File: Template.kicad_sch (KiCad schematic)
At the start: 0 parts

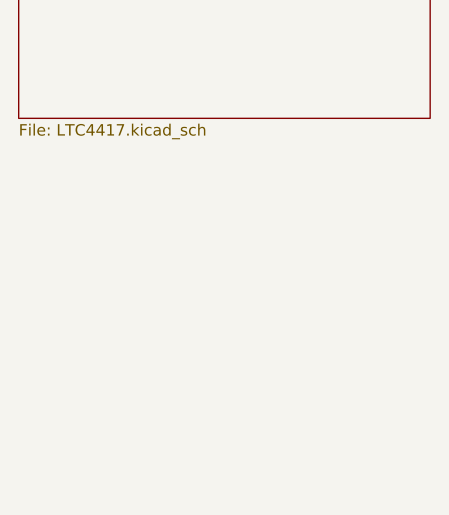
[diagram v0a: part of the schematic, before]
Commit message: add LTC4088
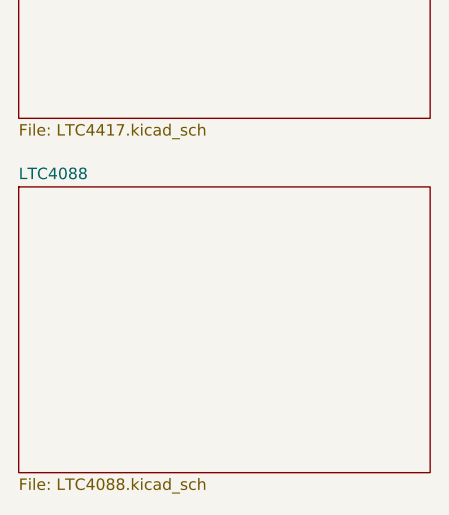
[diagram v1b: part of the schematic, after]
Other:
- added sheet LTC4088 (LTC4088.kicad_sch)
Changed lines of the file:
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@@
+		)
+	)
+	(sheet
+		(at 20.32 62.23)
+		(size 45.72 31.75)
+		(fields_autoplaced yes)
+		(stroke
+			(width 0.1524)
+			(type solid)
+		)
+		(fill
+			(color 255 255 194 1.0000)
+		)
+		(property "Sheetname" "LTC4088"
+			(at 20.32 61.5184 0)
+			(effects
+				(font
+					(size 1.27 1.27)
+				)
+				(justify left bottom)
+			)
+		)
+		(property "Sheetfile" "LTC4088.kicad_sch"
+			(at 20.32 94.5646 0)
+			(effects
+				(font
+					(size 1.27 1.27)
+				)
+				(justify left top)
+			)
+		)
+		(instances
+			(project "Template"
+				(path "/251827e7-9515-4eb7-984d-8b86837d4b30"
+					(page "3")
+				)
+			)
 		)
 	)

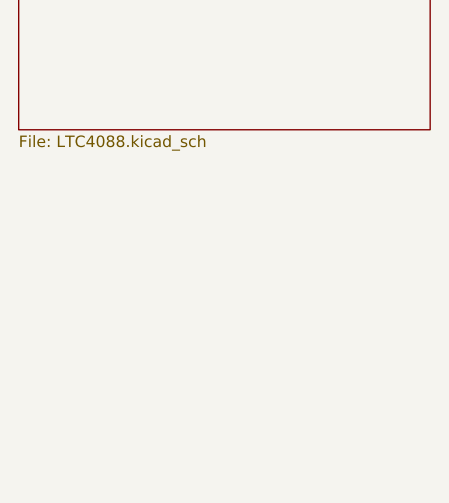
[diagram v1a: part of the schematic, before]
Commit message: add TPS63021 dcdc
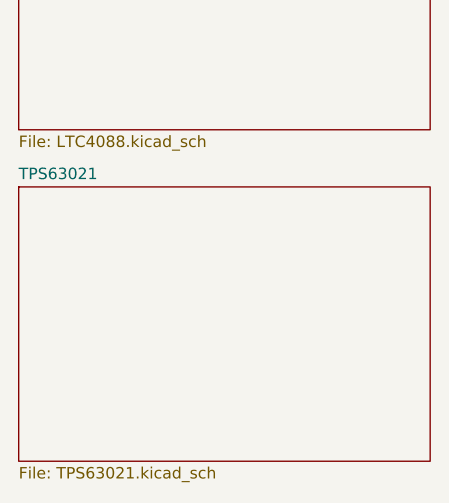
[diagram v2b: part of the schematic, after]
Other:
- added sheet TPS63021 (TPS63021.kicad_sch)
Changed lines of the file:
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@@
+		)
+	)
+	(sheet
+		(at 20.32 100.33)
+		(size 45.72 30.48)
+		(fields_autoplaced yes)
+		(stroke
+			(width 0.1524)
+			(type solid)
+		)
+		(fill
+			(color 255 255 194 1.0000)
+		)
+		(property "Sheetname" "TPS63021"
+			(at 20.32 99.6184 0)
+			(effects
+				(font
+					(size 1.27 1.27)
+				)
+				(justify left bottom)
+			)
+		)
+		(property "Sheetfile" "TPS63021.kicad_sch"
+			(at 20.32 131.3946 0)
+			(effects
+				(font
+					(size 1.27 1.27)
+				)
+				(justify left top)
+			)
+		)
+		(instances
+			(project "Template"
+				(path "/251827e7-9515-4eb7-984d-8b86837d4b30"
+					(page "4")
+				)
+			)
 		)
 	)

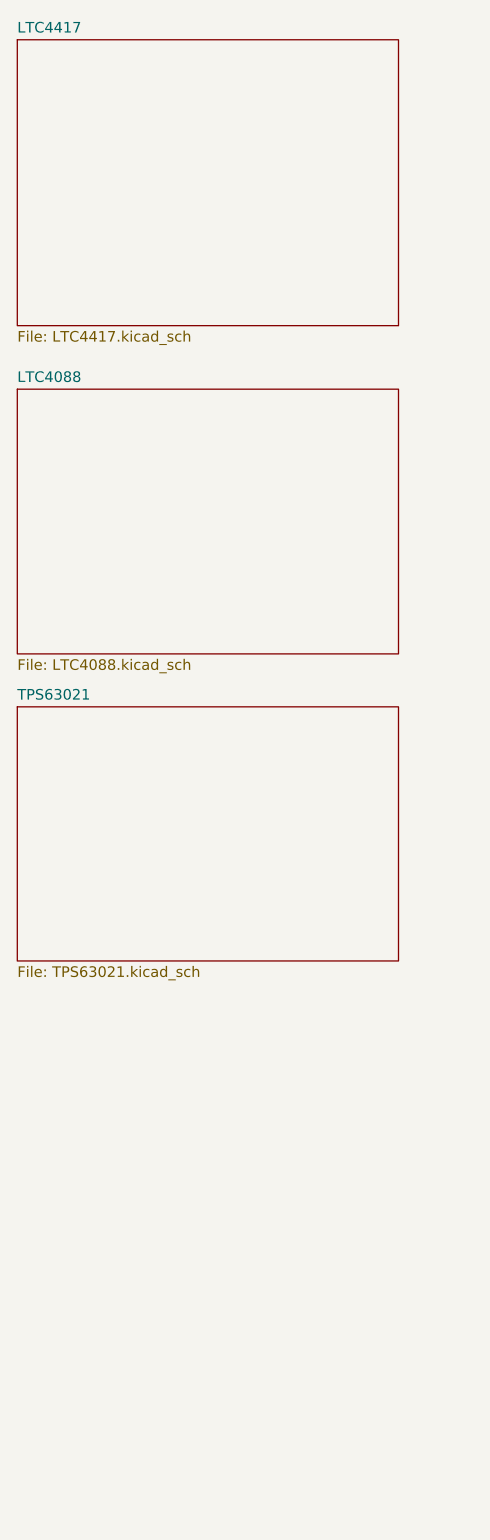
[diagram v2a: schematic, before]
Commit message: add footprint 18650 batteryClip
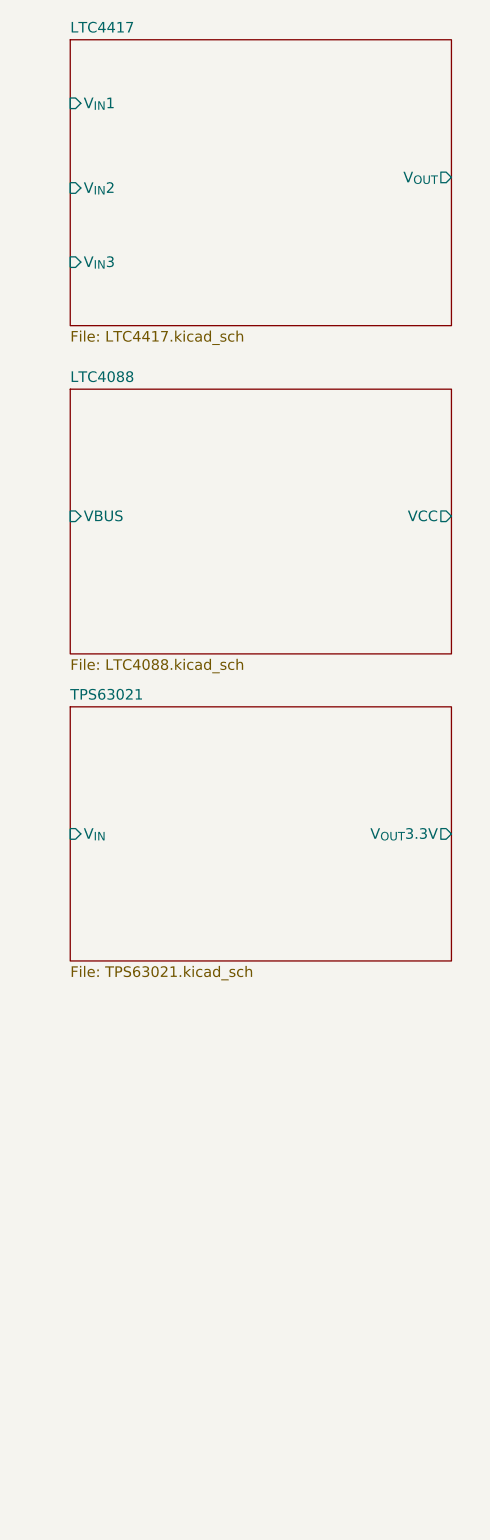
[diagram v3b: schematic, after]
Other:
- sheet LTC4088 ports: added VBUS, VCC; removed none
- sheet LTC4417 ports: added V_{IN}1, V_{IN}2, V_{IN}3, V_{OUT}; removed none
- sheet TPS63021 ports: added V_{IN}, V_{OUT}3.3V; removed none
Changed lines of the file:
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@@
 	(paper "A4")
 	(sheet
-		(at 20.32 20.32)
+		(at 26.67 20.32)
 		(size 45.72 34.29)
 		(fields_autoplaced yes)
@@
 		)
 		(property "Sheetname" "LTC4417"
-			(at 20.32 19.6084 0)
+			(at 26.67 19.6084 0)
 			(effects
 				(font
@@
 		)
 		(property "Sheetfile" "LTC4417.kicad_sch"
-			(at 20.32 55.1946 0)
+			(at 26.67 55.1946 0)
 			(effects
 				(font
@@
 				)
 				(justify left top)
+			)
+		)
+		(pin "V_{OUT}" output
+			(at 72.39 36.83 0)
+			(effects
+				(font
+					(size 1.27 1.27)
+				)
+				(justify right)
+			)
+		)
+		(pin "V_{IN}1" input
+			(at 26.67 27.94 180)
+			(effects
+				(font
+					(size 1.27 1.27)
+				)
+				(justify left)
+			)
+		)
+		(pin "V_{IN}2" input
+			(at 26.67 38.1 180)
+			(effects
+				(font
+					(size 1.27 1.27)
+				)
+				(justify left)
+			)
+		)
+		(pin "V_{IN}3" input
+			(at 26.67 46.99 180)
+			(effects
+				(font
+					(size 1.27 1.27)
+				)
+				(justify left)
 			)
 		)
@@
 	)
 	(sheet
-		(at 20.32 62.23)
+		(at 26.67 62.23)
 		(size 45.72 31.75)
 		(fields_autoplaced yes)
@@
 		)
 		(property "Sheetname" "LTC4088"
-			(at 20.32 61.5184 0)
+			(at 26.67 61.5184 0)
 			(effects
 				(font
@@
 		)
 		(property "Sheetfile" "LTC4088.kicad_sch"
-			(at 20.32 94.5646 0)
+			(at 26.67 94.5646 0)
 			(effects
 				(font
@@
 				)
 				(justify left top)
+			)
+		)
+		(pin "VCC" output
+			(at 72.39 77.47 0)
+			(effects
+				(font
+					(size 1.27 1.27)
+				)
+				(justify right)
+			)
+		)
+		(pin "VBUS" input
+			(at 26.67 77.47 180)
+			(effects
+				(font
+					(size 1.27 1.27)
+				)
+				(justify left)
 			)
 		)
@@
 	)
 	(sheet
-		(at 20.32 100.33)
+		(at 26.67 100.33)
 		(size 45.72 30.48)
 		(fields_autoplaced yes)
@@
 		)
 		(property "Sheetname" "TPS63021"
-			(at 20.32 99.6184 0)
+			(at 26.67 99.6184 0)
 			(effects
 				(font
@@
 		)
 		(property "Sheetfile" "TPS63021.kicad_sch"
-			(at 20.32 131.3946 0)
+			(at 26.67 131.3946 0)
 			(effects
 				(font
@@
 			)
 		)
+		(pin "V_{IN}" input
+			(at 26.67 115.57 180)
+			(effects
+				(font
+					(size 1.27 1.27)
+				)
+				(justify left)
+			)
+		)
+		(pin "V_{OUT}3.3V" output
+			(at 72.39 115.57 0)
+			(effects
+				(font
+					(size 1.27 1.27)
+				)
+				(justify right)
+			)
+		)

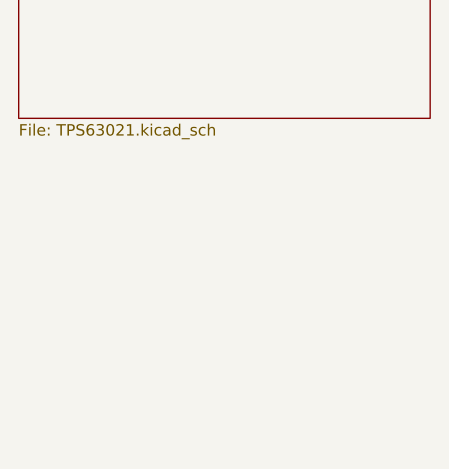
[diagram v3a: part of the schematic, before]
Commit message: add USB-PD sheet and TPD2E2U06DRLR symbol and footprint
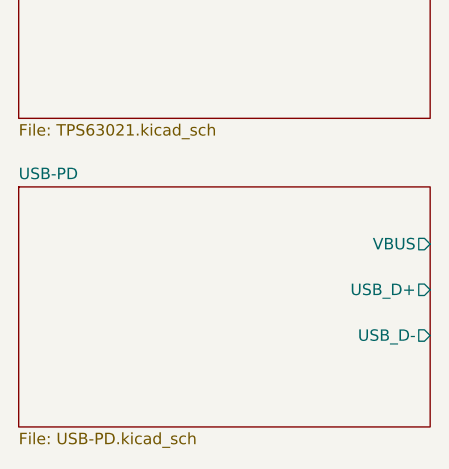
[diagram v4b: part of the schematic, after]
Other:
- added sheet USB-PD (USB-PD.kicad_sch)
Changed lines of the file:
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@@
+	)
+	(sheet
+		(at 26.67 138.43)
+		(size 45.72 26.67)
+		(fields_autoplaced yes)
+		(stroke
+			(width 0.1524)
+			(type solid)
+		)
+		(fill
+			(color 255 255 194 1.0000)
+		)
+		(property "Sheetname" "USB-PD"
+			(at 26.67 137.7184 0)
+			(effects
+				(font
+					(size 1.27 1.27)
+				)
+				(justify left bottom)
+			)
+		)
+		(property "Sheetfile" "USB-PD.kicad_sch"
+			(at 26.67 165.6846 0)
+			(effects
+				(font
+					(size 1.27 1.27)
+				)
+				(justify left top)
+			)
+		)
+		(pin "VBUS" output
+			(at 72.39 144.78 0)
+			(effects
+				(font
+					(size 1.27 1.27)
+				)
+				(justify right)
+			)
+		)
+		(pin "USB_D+" output
+			(at 72.39 149.86 0)
+			(effects
+				(font
+					(size 1.27 1.27)
+				)
+				(justify right)
+			)
+		)
+		(pin "USB_D-" output
+			(at 72.39 154.94 0)
+			(effects
+				(font
+					(size 1.27 1.27)
+				)
+				(justify right)
+			)
+		)
+		(instances
+			(project "Template"
+				(path "/251827e7-9515-4eb7-984d-8b86837d4b30"
+					(page "5")
+				)
+			)
+		)
 	)
 	(sheet

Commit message: add crystal
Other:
- added sheet Crystal (Crystal.kicad_sch)
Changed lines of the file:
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@@
+	)
+	(sheet
+		(at 26.67 171.45)
+		(size 48.26 24.13)
+		(fields_autoplaced yes)
+		(stroke
+			(width 0.1524)
+			(type solid)
+		)
+		(fill
+			(color 255 255 194 1.0000)
+		)
+		(property "Sheetname" "Crystal"
+			(at 26.67 170.7384 0)
+			(effects
+				(font
+					(size 1.27 1.27)
+				)
+				(justify left bottom)
+			)
+		)
+		(property "Sheetfile" "Crystal.kicad_sch"
+			(at 26.67 196.1646 0)
+			(effects
+				(font
+					(size 1.27 1.27)
+				)
+				(justify left top)
+			)
+		)
+		(instances
+			(project "Template"
+				(path "/251827e7-9515-4eb7-984d-8b86837d4b30"
+					(page "6")
+				)
+			)
+		)
 	)
 	(sheet
